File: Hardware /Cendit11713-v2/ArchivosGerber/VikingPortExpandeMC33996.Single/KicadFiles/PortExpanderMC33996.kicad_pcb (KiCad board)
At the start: 2 copper layers, 12 parts, among them J1 DEBUG_CONN, P1 VIKING_HEADER_9P, P2 VIKING_HEADER_9P, U1 MC33996EKR2

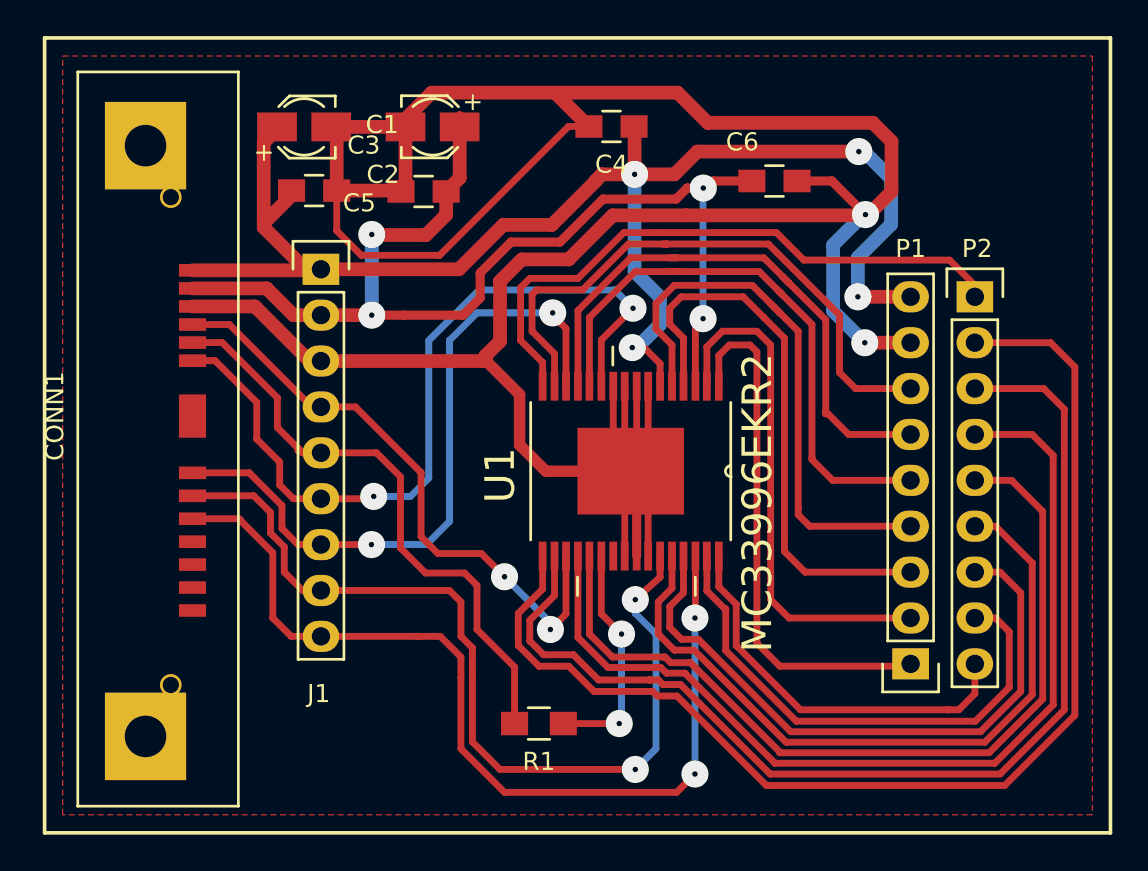
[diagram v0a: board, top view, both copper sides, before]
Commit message: En CenditLab.Reducido + Cendit11713
  - Para CenditLab vistas para Steps + fabrica de vistas ComponentViewfactory
  - En Cendit11713 revision PCB VikingPortExpander + Gerber
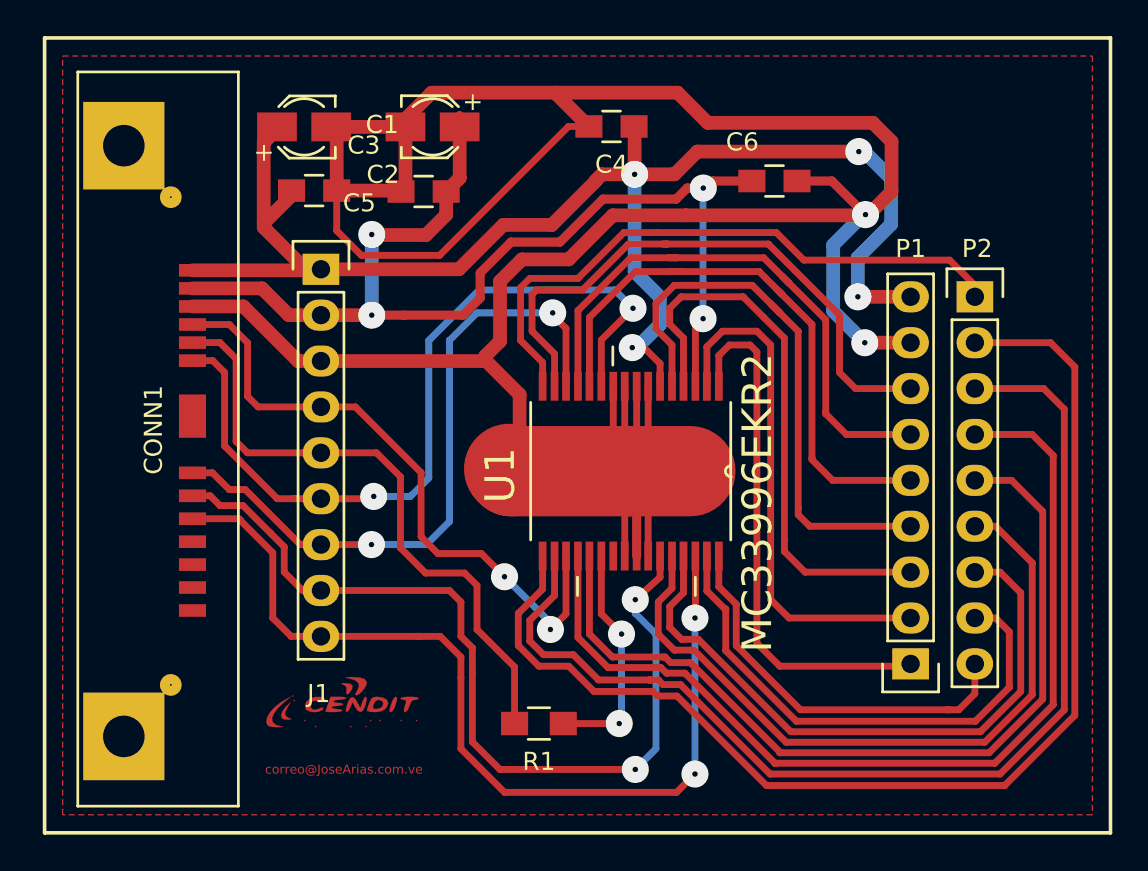
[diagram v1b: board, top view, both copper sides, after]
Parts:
- added G1: LOGO, CenditFootprints:CENDIT_LOGO_SOLDER, F.Cu at (108.3, 114.8)
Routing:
- net GNDPWR: track 179.7 -> 190.4 mm
- net /MISO: track 33.5 -> 35.8 mm
- net /MOSI: track 33.7 -> 36.0 mm
- net //CS: track 37.9 -> 37.1 mm
- net /SCLK: track 44.5 -> 45.2 mm
- net //RESET: track 49.8 -> 49.1 mm
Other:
- board text added: "correo@JoseArias.com.ve"
